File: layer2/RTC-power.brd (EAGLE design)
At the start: 17.8 x 49.5 mm, 15 parts, among them U1 DS3234, U2 MCP73831

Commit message: final chnages before ordering
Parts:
- moved C4 0.63 mm to (12.1, 47.0)
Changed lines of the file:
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@@
 <setting verticaltext="up"/>
 </settings>
-<grid distance="0.05" unitdist="inch" unit="inch" style="lines" multiple="1" display="yes" altdistance="0.005" altunitdist="inch" altunit="inch"/>
+<grid distance="0.025" unitdist="inch" unit="inch" style="lines" multiple="1" display="yes" altdistance="0.005" altunitdist="inch" altunit="inch"/>
 <layers>
 <layer number="1" name="Top" color="4" fill="1" visible="yes" active="yes"/>
@@
 </autorouter>
 <elements>
-<element name="BAT1" library="SparkFun" package="BATTCON_12MM_CURVED" value="3V" x="7.62" y="24.13" rot="R90"/>
-<element name="D11" library="SparkFun-LED" package="LED-0603" value="RED" x="10.16" y="12.7" rot="R270">
+<element name="BAT1" library="SparkFun" package="BATTCON_12MM_CURVED" value="3V" x="7.62" y="24.13" smashed="yes" rot="R90"/>
+<element name="D11" library="SparkFun-LED" package="LED-0603" value="RED" x="10.16" y="12.7" smashed="yes" rot="R270">
 <attribute name="PROD_ID" value="DIO-00819" x="10.16" y="12.7" size="1.778" layer="27" rot="R270" display="off"/>
-</element>
-<element name="J2" library="SparkFun-Connectors" package="1X12" value="" x="16.51" y="45.72" rot="R270"/>
-<element name="JP1" library="SparkFun-Connectors" package="JST-2-SMD@1" value="JST" x="8.89" y="16.51" rot="MR0">
+<attribute name="VALUE" x="9.144" y="11.6205" size="0.4064" layer="27"/>
+</element>
+<element name="J2" library="SparkFun-Connectors" package="1X12" value="" x="16.51" y="45.72" smashed="yes" rot="R270">
+<attribute name="VALUE" x="13.335" y="46.99" size="1.27" layer="27" rot="R270"/>
+</element>
+<element name="JP1" library="SparkFun-Connectors" package="JST-2-SMD@1" value="JST" x="8.89" y="16.51" smashed="yes" rot="MR0">
 <attribute name="PROD_ID" value="CONN-08352" x="8.89" y="16.51" size="1.778" layer="28" rot="MR0" display="off"/>
-</element>
-<element name="JP9" library="SparkFun-Connectors" package="USB-AB-MICRO-SMD_V03" value="Micro USB" x="7.62" y="2.54" rot="R90">
+<attribute name="VALUE" x="10.16" y="16.51" size="0.4064" layer="28" rot="MR0"/>
+</element>
+<element name="JP9" library="SparkFun-Connectors" package="USB-AB-MICRO-SMD_V03" value="Micro USB" x="7.62" y="2.54" smashed="yes" rot="R90">
 <attribute name="PROD_ID" value="CONN-11794" x="7.62" y="2.54" size="1.778" layer="27" rot="R90" display="off"/>
-</element>
-<element name="U1" library="SparkFun" package="DS3234" value="DS3234" x="8.89" y="40.64" rot="R180"/>
-<element name="U2" library="SparkFun-PowerIC" package="SOT23-5" value="MCP73831" x="13.97" y="11.43" rot="R270">
+<attribute name="VALUE" x="2.159" y="1.27" size="0.4064" layer="27" rot="R90"/>
+</element>
+<element name="U1" library="SparkFun" package="DS3234" value="DS3234" x="8.89" y="40.64" smashed="yes" rot="R180"/>
+<element name="U2" library="SparkFun-PowerIC" package="SOT23-5" value="MCP73831" x="13.97" y="11.43" smashed="yes" rot="R270">
 <attribute name="PROD_ID" value="IC-09995" x="13.97" y="11.43" size="1.778" layer="27" rot="R270" display="off"/>
-</element>
-<element name="R1" library="microbuilder" package="_0805MP" value="10K" x="7.62" y="48.26" rot="R180"/>
-<element name="R3" library="microbuilder" package="_0805MP" value="330" x="8.89" y="8.89" rot="R90"/>
-<element name="R2" library="microbuilder" package="_0805MP" value="2.0k" x="13.97" y="15.24"/>
-<element name="C2" library="microbuilder" package="0805-NO" value="4.7uF" x="15.24" y="5.08" rot="R90"/>
-<element name="C3" library="microbuilder" package="0805-NO" value="4.7uF" x="13.97" y="8.89"/>
-<element name="C4" library="SparkFun" package="0402-CAP" value="22pF" x="11.43" y="46.99"/>
-<element name="J3" library="SparkFun-Connectors" package="1X01" value="" x="1.27" y="17.78"/>
-<element name="J4" library="SparkFun-Connectors" package="1X07" value="" x="1.27" y="30.48" rot="R90"/>
+<attribute name="VALUE" x="13.7795" y="12.3825" size="0.4064" layer="27" rot="R270"/>
+</element>
+<element name="R1" library="microbuilder" package="_0805MP" value="10K" x="7.62" y="48.26" smashed="yes" rot="R180">
+<attribute name="VALUE" x="9.2075" y="49.53" size="0.4064" layer="27" ratio="10" rot="R180"/>
+</element>
+<element name="R3" library="microbuilder" package="_0805MP" value="330" x="8.89" y="8.89" smashed="yes" rot="R90">
+<attribute name="VALUE" x="10.16" y="7.3025" size="0.4064" layer="27" ratio="10" rot="R90"/>
+</element>
+<element name="R2" library="microbuilder" package="_0805MP" value="2.0k" x="13.97" y="15.24" smashed="yes">
+<attribute name="VALUE" x="12.3825" y="13.97" size="0.4064" layer="27" ratio="10"/>
+</element>
+<element name="C2" library="microbuilder" package="0805-NO" value="4.7uF" x="15.24" y="5.08" smashed="yes" rot="R90">
+<attribute name="VALUE" x="16.002" y="7.112" size="0.4064" layer="27" ratio="10" rot="R90"/>
+</element>
+<element name="C3" library="microbuilder" package="0805-NO" value="4.7uF" x="13.97" y="8.89" smashed="yes">
+<attribute name="VALUE" x="16.002" y="8.128" size="0.4064" layer="27" ratio="10"/>
+</element>
+<element name="C4" library="SparkFun" package="0402-CAP" value="22pF" x="12.065" y="46.99" smashed="yes">
+<attribute name="VALUE" x="10.9855" y="45.847" size="0.4064" layer="27"/>
+</element>
+<element name="J3" library="SparkFun-Connectors" package="1X01" value="" x="1.27" y="17.78" smashed="yes">
+<attribute name="VALUE" x="0" y="14.605" size="1.27" layer="27"/>
+</element>
+<element name="J4" library="SparkFun-Connectors" package="1X07" value="" x="1.27" y="30.48" smashed="yes" rot="R90">
+<attribute name="VALUE" x="4.445" y="29.21" size="1.27" layer="27" rot="R90"/>
+</element>
 </elements>
 <signals>
@@
 <via x="5.08" y="31.75" extent="1-16" drill="0.508"/>
 <contactref element="C4" pad="2"/>
-<wire x1="13.335" y1="45.325" x2="13.335" y2="45.735" width="0.254" layer="1"/>
-<wire x1="13.335" y1="45.735" x2="12.08" y2="46.99" width="0.254" layer="1"/>
 <wire x1="13.335" y1="45.325" x2="13.335" y2="43.815" width="0.254" layer="1"/>
 <via x="11.43" y="41.91" extent="1-16" drill="0.508"/>
@@
 <via x="11.43" y="2.54" extent="1-16" drill="0.508"/>
 <wire x1="14.92" y1="8.89" x2="14.92" y2="8.57" width="0.4064" layer="1"/>
+<wire x1="13.335" y1="45.325" x2="13.335" y2="46.37" width="0.254" layer="1"/>
+<wire x1="13.335" y1="46.37" x2="12.715" y2="46.99" width="0.254" layer="1"/>
 </signal>
 <signal name="MISO">
@@
 <wire x1="8.636" y1="48.26" x2="11.43" y2="48.26" width="0.254" layer="1"/>
 <wire x1="11.43" y1="48.26" x2="15.24" y2="48.26" width="0.254" layer="1"/>
-<wire x1="10.78" y1="46.99" x2="10.78" y2="45.34" width="0.254" layer="1"/>
 <wire x1="10.78" y1="45.34" x2="10.795" y2="45.325" width="0.254" layer="1"/>
 <wire x1="16.51" y1="38.1" x2="15.24" y2="39.37" width="0.254" layer="1"/>
-<wire x1="10.78" y1="46.99" x2="10.78" y2="47.61" width="0.254" layer="1"/>
-<wire x1="10.78" y1="47.61" x2="11.43" y2="48.26" width="0.254" layer="1"/>
+<wire x1="10.78" y1="45.34" x2="10.78" y2="46.355" width="0.254" layer="1"/>
+<wire x1="10.78" y1="46.355" x2="11.415" y2="46.99" width="0.254" layer="1"/>
+<wire x1="11.415" y1="46.99" x2="11.415" y2="48.245" width="0.254" layer="1"/>
+<wire x1="11.415" y1="48.245" x2="11.43" y2="48.26" width="0.254" layer="1"/>
 </signal>
 <signal name="N$3">

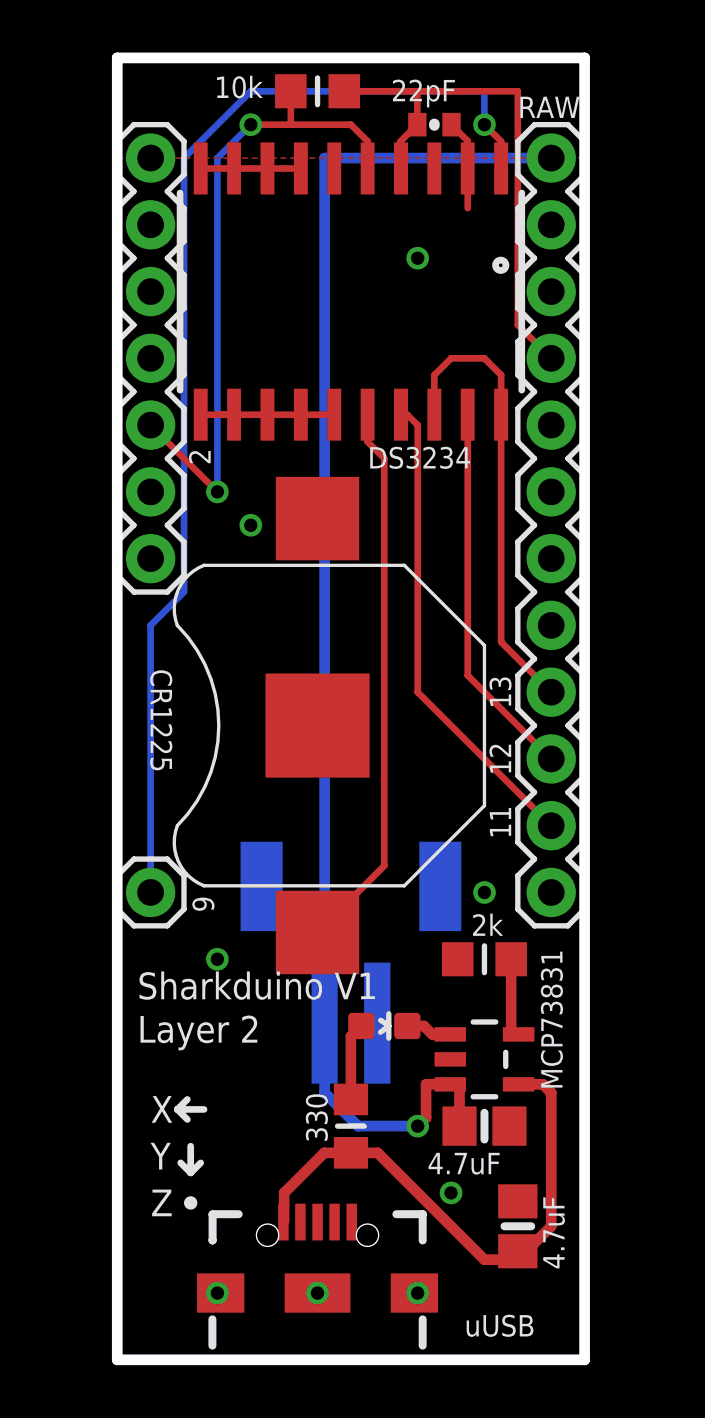
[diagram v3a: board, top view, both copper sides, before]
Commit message: removed pin 4, movved batt holder
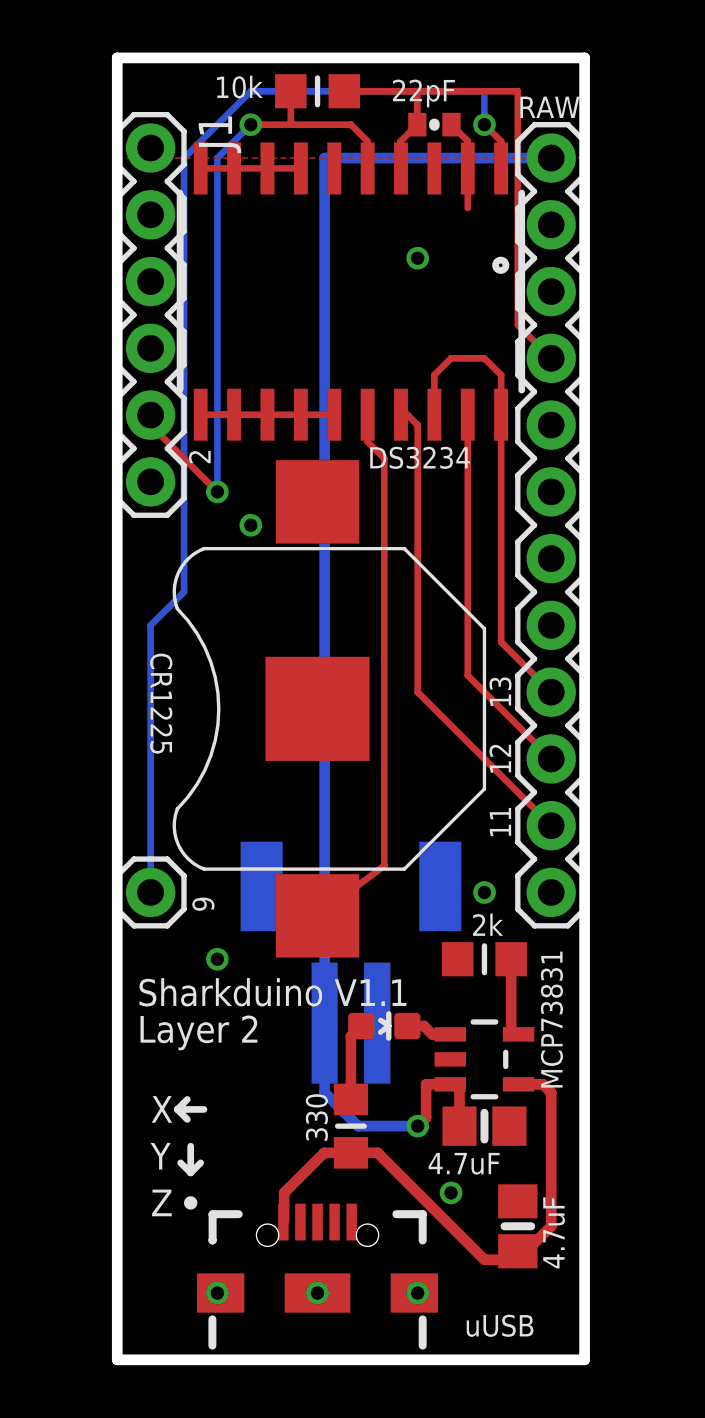
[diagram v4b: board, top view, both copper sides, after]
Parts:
- removed J4: (no value), SparkFun-Connectors:1X07
- added J1: (no value), SparkFun-Connectors:1X06
- moved BAT1 0.64 mm to (7.62, 24.8)
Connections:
- net GND: no longer J4.4
- net INT/SQW: no longer J4.3
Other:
- board text added: "Sharkduino V1.1"
- board text added: "Sharkduino V1.1 Layer 2"
- board text removed: "Shankduino V1 Layer 2"
- board text removed: "Sharkduino V1"
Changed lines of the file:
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@@
 <text x="14.986" y="24.765" size="0.8128" layer="21" font="vector" ratio="15" rot="R90">13</text>
 <text x="15.24" y="47.244" size="0.8128" layer="21" font="vector" ratio="15">RAW</text>
-<text x="1.27" y="26.289" size="0.8128" layer="21" font="vector" ratio="15" rot="SR270">CR1225</text>
+<text x="1.27" y="26.924" size="0.8128" layer="21" font="vector" ratio="15" rot="SR270">CR1225</text>
 <text x="3.556" y="34.036" size="0.8128" layer="21" font="vector" ratio="15" rot="R90">2</text>
 <text x="17.018" y="3.429" size="0.8128" layer="21" font="vector" ratio="15" rot="R90">4.7uF</text>
@@
 <text x="9.525" y="33.909" size="0.8128" layer="21" font="vector" ratio="15">DS3234</text>
 <text x="16.129" y="15.621" size="0.8128" layer="21" font="vector" ratio="15" rot="R270">MCP73831</text>
-<text x="0.762" y="13.716" size="1.016" layer="21" font="vector" ratio="15">Sharkduino V1</text>
+<text x="0.762" y="13.462" size="1.016" layer="21" font="vector" ratio="15">Sharkduino V1.1</text>
 <text x="0.762" y="12.065" size="1.016" layer="21" font="vector" ratio="15">Layer 2</text>
 <text x="13.208" y="0.889" size="0.8128" layer="21" font="vector" ratio="15">uUSB</text>
@@
 <text x="13.208" y="40.386" size="1.016" layer="22" font="vector" ratio="15" rot="MR270">William Laney  2016</text>
 <text x="8.89" y="40.386" size="1.016" layer="22" font="vector" ratio="15" rot="MR270">W&amp;M Physics   VIMS</text>
-<text x="6.731" y="40.386" size="1.016" layer="22" font="vector" ratio="15" rot="MR270">Shankduino V1 Layer 2</text>
+<text x="6.731" y="40.386" size="1.016" layer="22" font="vector" ratio="15" rot="MR270">Sharkduino V1.1 Layer 2</text>
 <text x="11.049" y="40.386" size="1.016" layer="22" font="vector" ratio="15" rot="MR270">welaney@email.wm.edu</text>
 </plain>
@@
 </autorouter>
 <elements>
-<element name="BAT1" library="SparkFun" package="BATTCON_12MM_CURVED" value="3V" x="7.62" y="24.13" smashed="yes" rot="R90"/>
+<element name="BAT1" library="SparkFun" package="BATTCON_12MM_CURVED" value="3V" x="7.62" y="24.765" smashed="yes" rot="R90"/>
 <element name="D11" library="SparkFun-LED" package="LED-0603" value="RED" x="10.16" y="12.7" smashed="yes" rot="R270">
 <attribute name="PROD_ID" value="DIO-00819" x="10.16" y="12.7" size="1.778" layer="27" rot="R270" display="off"/>
@@
 <attribute name="VALUE" x="0" y="14.605" size="1.27" layer="27"/>
 </element>
-<element name="J4" library="SparkFun-Connectors" package="1X07" value="" x="1.27" y="30.48" smashed="yes" rot="R90">
-<attribute name="VALUE" x="4.445" y="29.21" size="1.27" layer="27" rot="R90"/>
+<element name="J1" library="SparkFun-Connectors" package="1X06" value="" x="1.27" y="46.101" rot="R270">
+<attribute name="PROD_ID" value="CONN-08437" x="1.27" y="46.101" size="1.778" layer="27" font="vector" ratio="15" rot="R270" display="off"/>
 </element>
 </elements>
@@
 <via x="13.97" y="17.78" extent="1-16" drill="0.508"/>
 <via x="12.7" y="6.35" extent="1-16" drill="0.508"/>
-<contactref element="J4" pad="4"/>
 <via x="3.81" y="2.54" extent="1-16" drill="0.508"/>
 <via x="7.62" y="2.54" extent="1-16" drill="0.508"/>
@@
 <wire x1="6.604" y1="46.99" x2="6.604" y2="48.26" width="0.254" layer="1"/>
 <wire x1="6.604" y1="46.99" x2="5.08" y2="46.99" width="0.254" layer="1"/>
-<contactref element="J4" pad="3"/>
 <wire x1="3.81" y1="45.72" x2="5.08" y2="46.99" width="0.254" layer="16"/>
-<wire x1="1.27" y1="35.56" x2="1.397" y2="35.56" width="0.254" layer="1"/>
 <wire x1="1.397" y1="35.56" x2="1.397" y2="35.433" width="0.254" layer="1"/>
 <wire x1="1.397" y1="35.433" x2="3.81" y2="33.02" width="0.254" layer="1"/>
@@
 <wire x1="9.525" y1="34.925" x2="10.16" y2="34.29" width="0.254" layer="1"/>
 <wire x1="10.16" y1="34.29" x2="10.16" y2="18.796" width="0.254" layer="1"/>
-<wire x1="10.16" y1="18.796" x2="7.62" y2="16.256" width="0.254" layer="1"/>
+<wire x1="10.16" y1="18.796" x2="7.62" y2="16.891" width="0.254" layer="1"/>
 </signal>
 <signal name="+3V3">
